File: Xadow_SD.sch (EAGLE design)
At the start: 4 parts, among them IC1 4050D, J1 MICRO-SDCARD-CONNECTOR-330006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, J2 12p FPC bottom contact, J3 12p FPC bottom contact

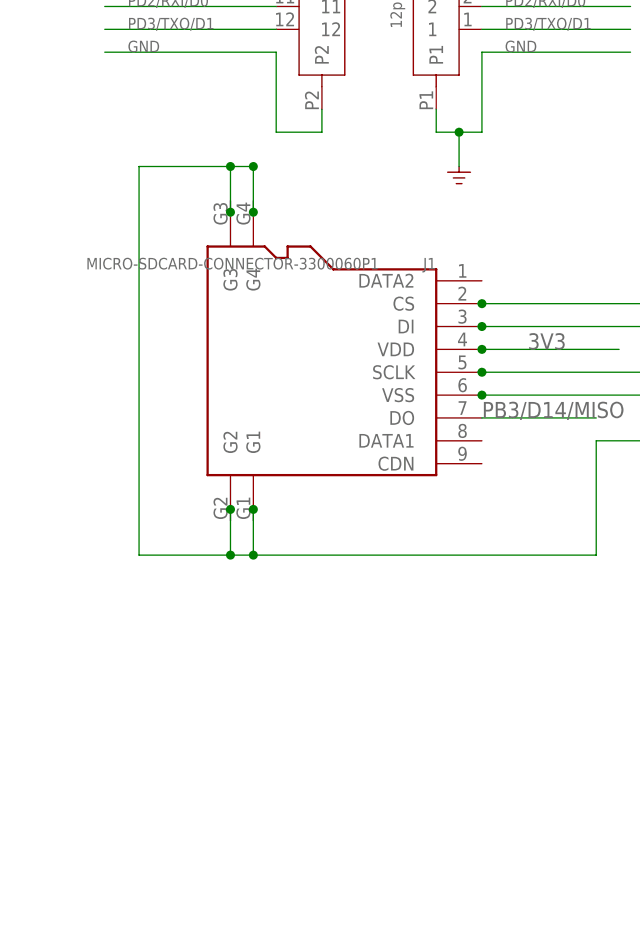
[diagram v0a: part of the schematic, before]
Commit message: Add 6-pin header
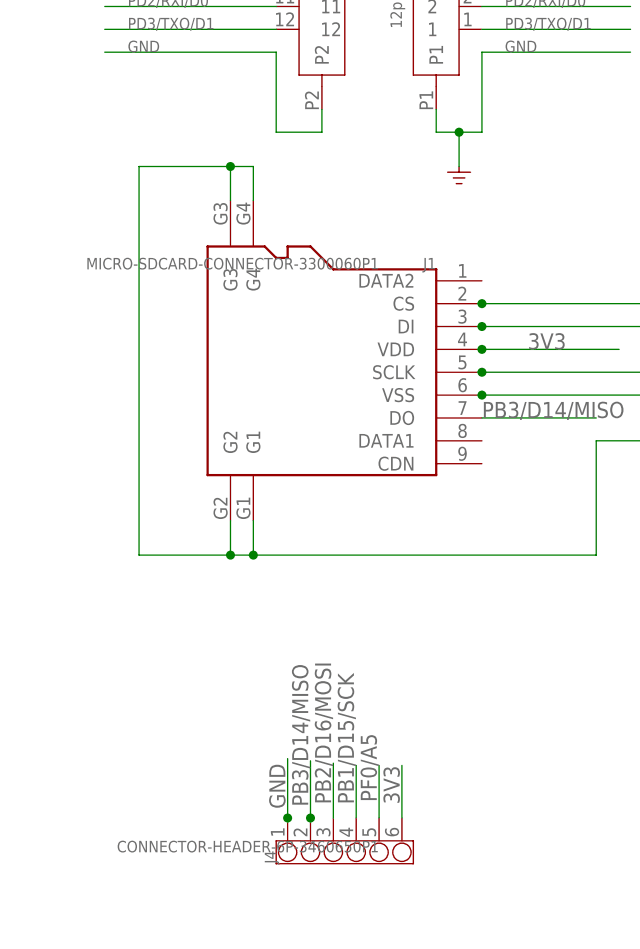
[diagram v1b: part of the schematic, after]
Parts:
- added J4: CONNECTOR-HEADER-6P-3460650P1, OPL:CONNECTOR-HEADER-6P-3460650P1
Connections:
- net 3V3: now also J4.6
- net GND: now also J1.G1, J1.G2, J1.G3, J1.G4, J4.1
- net PB1/D15/SCK: now also J4.4
- net PB2/D16/MOSI: now also J4.3
- net PB3/D14/MISO: now also J4.2
- net PF0/A5: now also J4.5

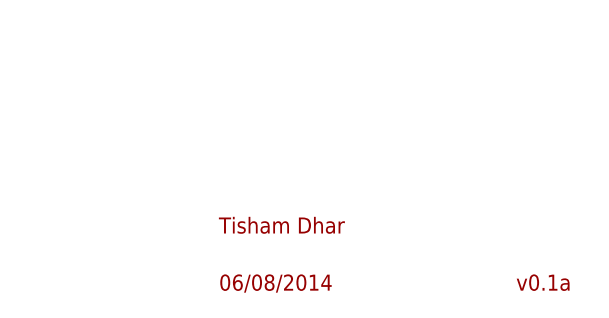
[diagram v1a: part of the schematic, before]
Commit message: Add labels and move graphics
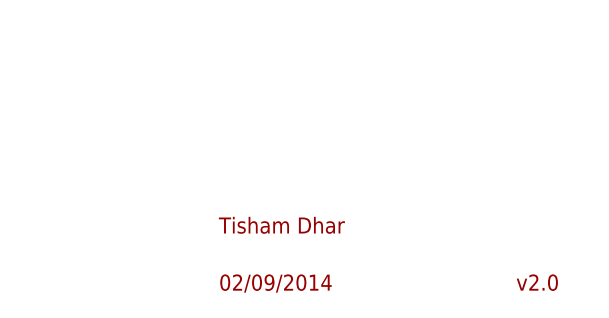
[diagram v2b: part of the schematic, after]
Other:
- note added: "02/09/2014"
- note added: "v2.0"
- note removed: "06/08/2014"
- note removed: "v0.1a"
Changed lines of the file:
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@@
 <plain>
 <text x="191.77" y="11.43" size="1.778" layer="94" ratio="10">Tisham Dhar</text>
-<text x="191.77" y="5.08" size="1.778" layer="94" ratio="10">06/08/2014</text>
-<text x="224.79" y="5.08" size="1.778" layer="94" ratio="10">v0.1a</text>
+<text x="191.77" y="5.08" size="1.778" layer="94" ratio="10">02/09/2014</text>
+<text x="224.79" y="5.08" size="1.778" layer="94" ratio="10">v2.0</text>
 </plain>
 <instances>
